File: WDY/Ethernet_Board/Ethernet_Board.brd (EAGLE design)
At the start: 41 x 57 mm, 35 parts, among them J1 22-05-7028-02, J2 22-05-7108-10, P1 RB1-125BAG1A, T1 EXMACHINA-LOGO-NAME, X1 ASE_50

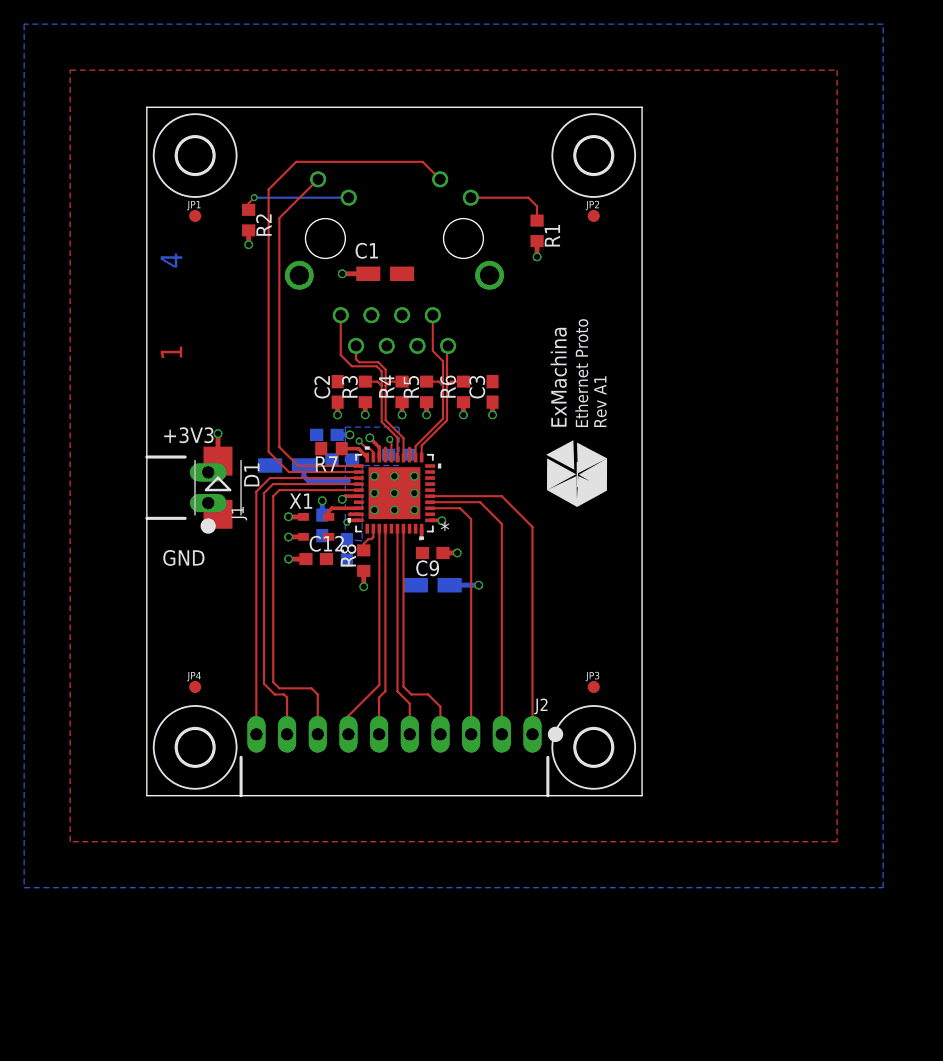
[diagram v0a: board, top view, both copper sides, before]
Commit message: Rotate 90 the board
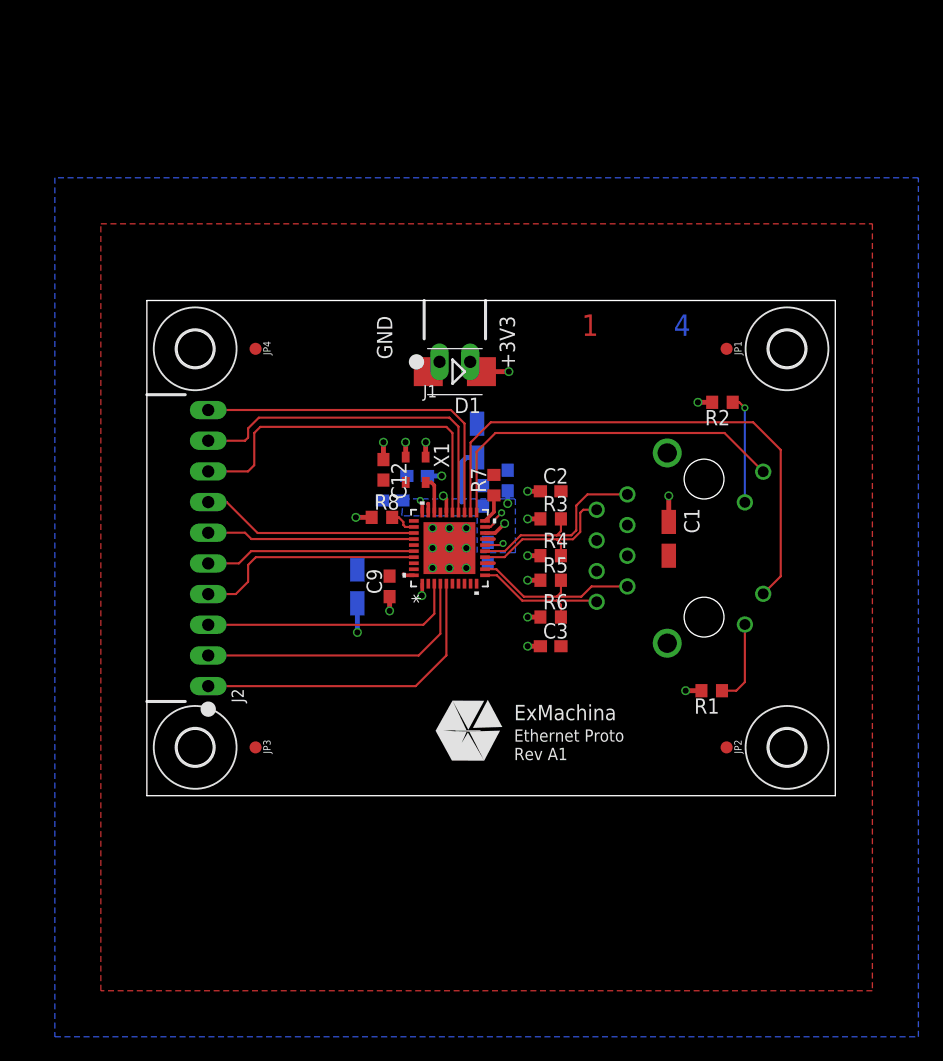
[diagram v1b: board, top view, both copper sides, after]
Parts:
- moved MP1 51.5 mm to (53.0, 4.00), turned to 0 degrees
- moved MP3 51.5 mm to (53.0, 37.0), turned to 0 degrees
- moved JP1 45.4 mm to (48.0, 37.0), turned to 270 degrees
- moved JP2 45.4 mm to (48.0, 4.00), turned to 270 degrees
- moved R2 42.0 mm to (47.7, 32.6), turned to 180 degrees
- moved R1 40.7 mm to (46.8, 8.69), turned to 180 degrees
- moved P1 36.2 mm to (46.1, 20.5), turned to 270 degrees
- moved MP2 33.0 mm to (4.00, 4.00), turned to 0 degrees
- moved MP4 33.0 mm to (4.00, 37.0), turned to 270 degrees
- moved C1 32.1 mm to (43.2, 21.3), turned to 270 degrees
- moved JP3 28.4 mm to (9.00, 4.00), turned to 270 degrees
- moved JP4 28.4 mm to (9.00, 37.0), turned to 270 degrees
- moved T1 23.1 mm to (26.6, 5.36), turned to 0 degrees
- moved J1 22.9 mm to (25.5, 35.9), turned to 180 degrees
- moved D1 21.8 mm to (25.5, 35.1), turned to 180 degrees
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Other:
- board size 41 x 57 mm -> 57 x 41 mm

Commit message: Split 12pts connectors on to 2x6pts connectors Adding 50MHz on output connector
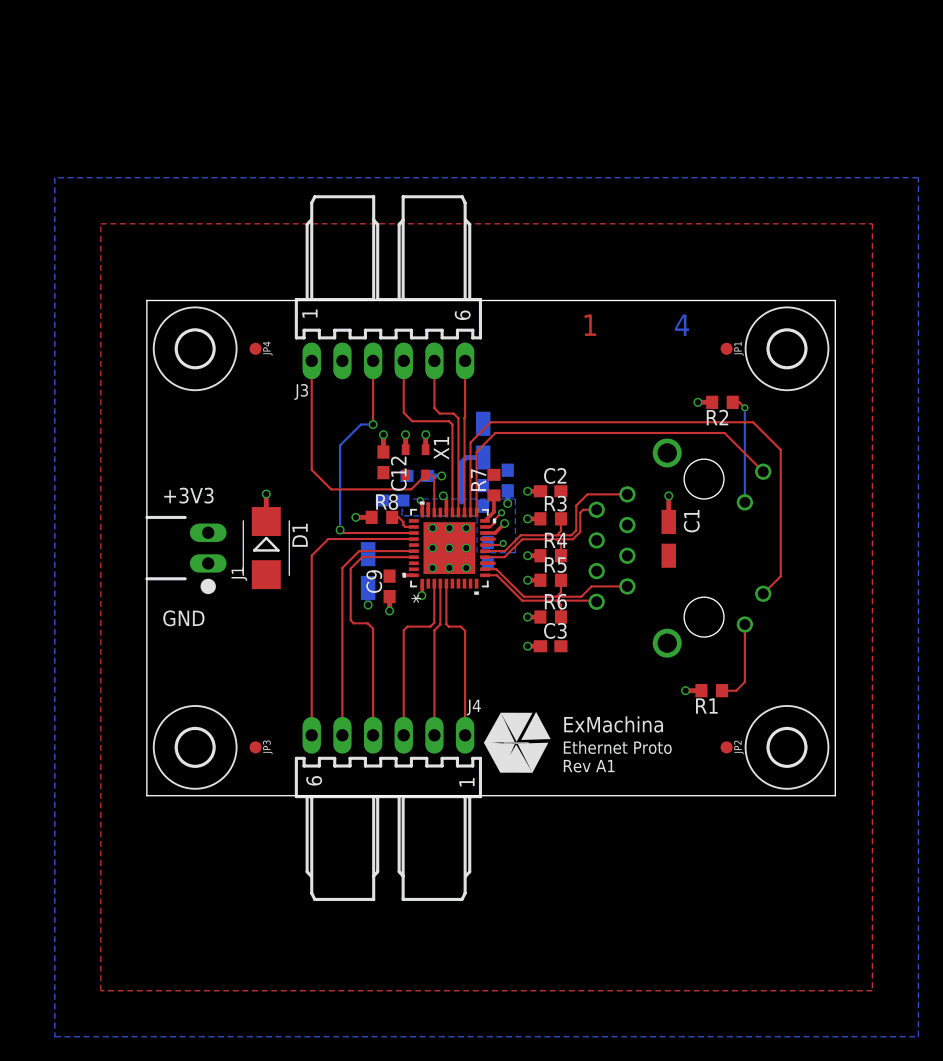
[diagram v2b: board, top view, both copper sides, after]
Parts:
- removed J2: 22-05-7108-10, con-molex:7395-10
- added J3, J4: 22-05-7068-06, con-molex:7395-06
- moved J1 25.6 mm to (5.08, 20.5), turned to 270 degrees
- moved D1 21.4 mm to (9.89, 20.5), turned to 270 degrees
- moved T1 4.12 mm to (30.6, 4.36)
- moved C8 1.55 mm to (18.3, 18.6)
- moved C12 0.62 mm to (19.6, 27.6)
- moved X1 0.62 mm to (22.3, 27.6)
- moved C4 0.51 mm to (27.8, 29.4)
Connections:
- net ETH_CRS: now also J3.3; no longer J2.7
- net ETH_MDC: now also J3.4; no longer J2.8
- net ETH_MDIO: now also J3.5; no longer J2.9
- net ETH_RST: now also J3.6; no longer J2.10
- net ETH_RXD_0: now also J4.5; no longer J2.5
- net ETH_RXD_1: now also J4.4; no longer J2.4
- net ETH_RX_ER: now also J4.6; no longer J2.6
- net ETH_TXD_0: now also J4.2; no longer J2.2
- net ETH_TXD_1: now also J4.1; no longer J2.1
- net ETH_TXD_EN: now also J4.3; no longer J2.3
- net ETH_X1: now also J3.1
- net GND: now also J3.2
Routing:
- net ETH_X1: track 3.06 -> 23.3 mm
- net ETH_RST: track 29.1 -> 12.6 mm
- net ETH_MDIO: track 29.4 -> 14.0 mm
- net ETH_MDC: track 30.1 -> 16.0 mm
- net ETH_TXD_1: track 26.7 -> 13.8 mm
- net ETH_TXD_0: track 24.1 -> 12.8 mm
- net ETH_TXD_EN: track 21.6 -> 14.7 mm
- net ETH_RX_ER: track 17.2 -> 23.9 mm
- net ETH_CRS: track 18.1 -> 21.9 mm, vias 0 -> 2
- net ETH_RXD_0: track 17.4 -> 20.3 mm
- net ETH_RXD_1: track 19.1 -> 20.9 mm
- net +3V3: track 28.8 -> 27.8 mm
- net PFBOUT: track 9.35 -> 9.86 mm
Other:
- board text added: "50MHz"
